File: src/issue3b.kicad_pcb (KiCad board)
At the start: 2 copper layers, 213.1 x 129 mm, 201 parts, among them IC1 ULA, IC10 4116, IC11 4116, IC12 4116, IC13 4116, IC14 LM1889, IC15 4532, IC16 4532, IC17 4532, IC18 4532, IC19 4532, IC2 Z80, IC20 4532, IC21 4532, IC22 4532, IC23 LS32, IC24 LS00, IC25 LS157, IC26 LS157, IC3 LS157, IC4 LS157, IC5 ROM, IC6 4116, IC7 4116, IC8 4116, IC9 4116, J7 Barrel_Jack_MountingPin, T1 Transformer_1P_1S, X1 14Mhz, X2 4.43Mhz

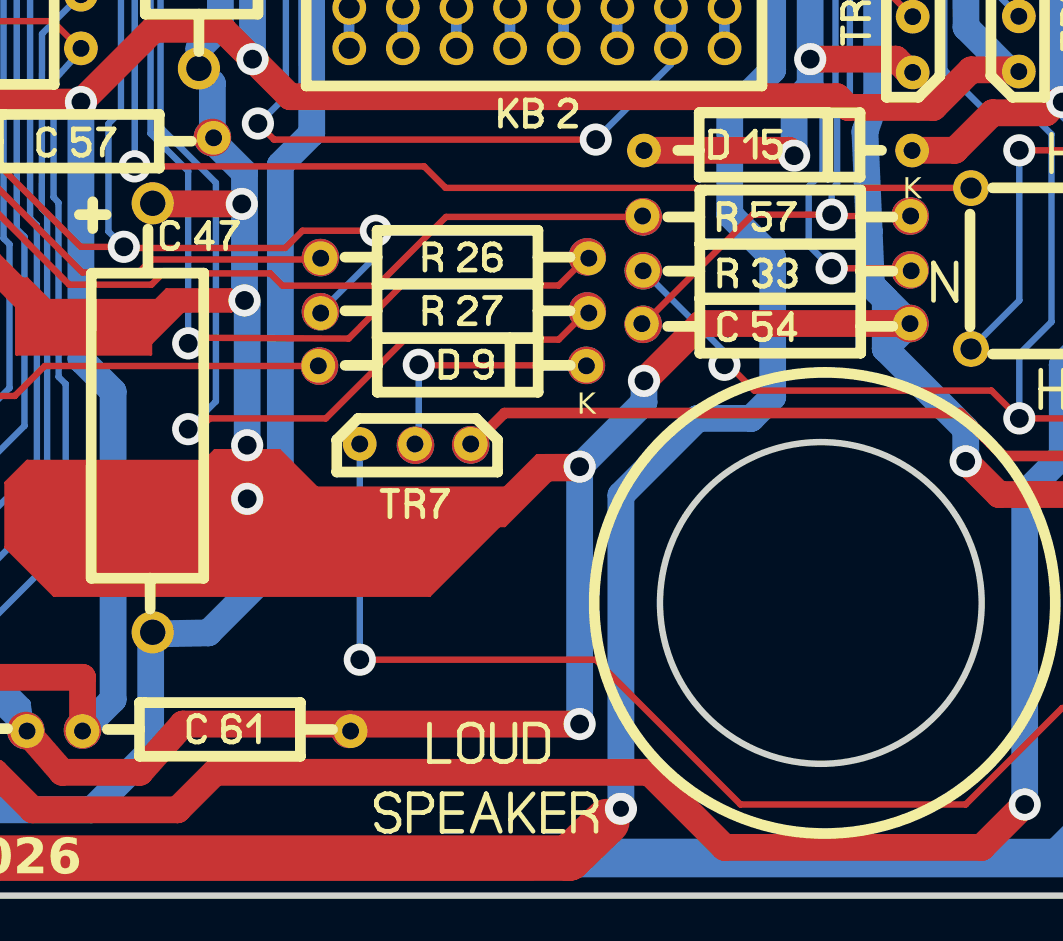
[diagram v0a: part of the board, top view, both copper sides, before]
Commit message: extra 3d parts from Dee inc heat sink.
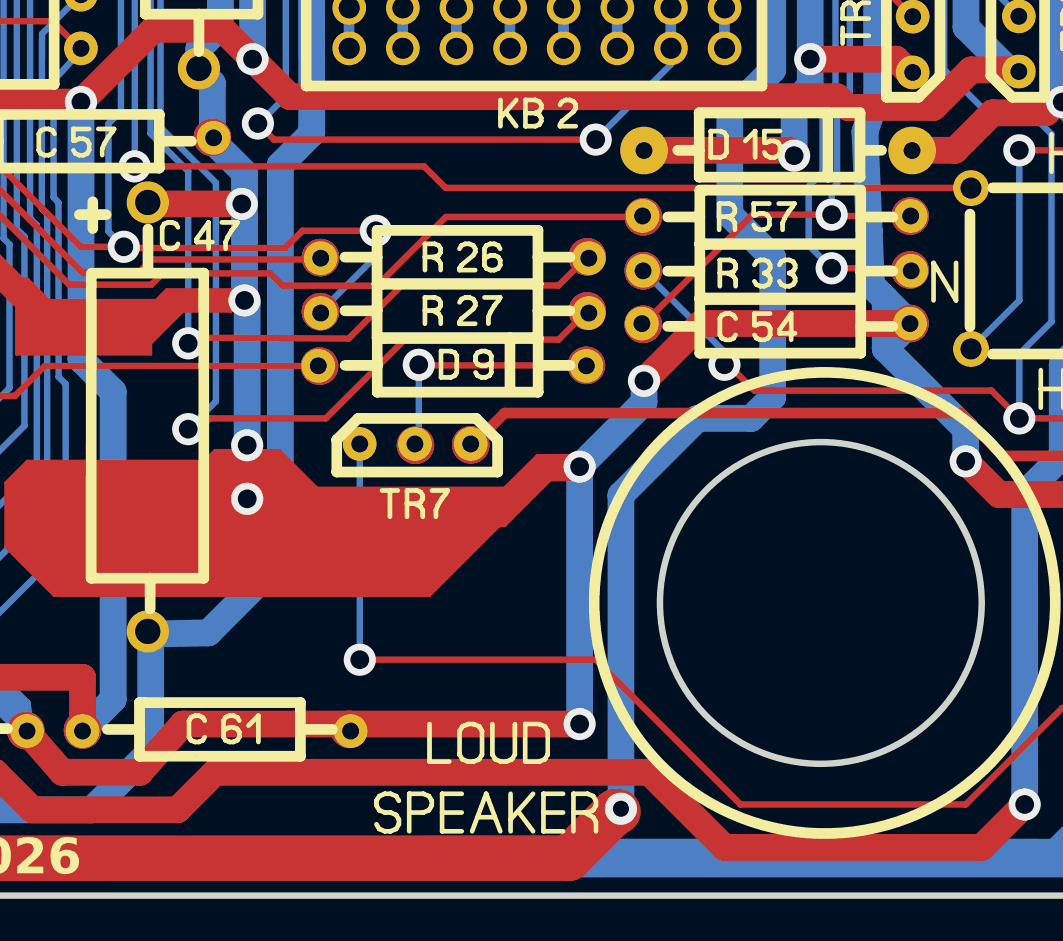
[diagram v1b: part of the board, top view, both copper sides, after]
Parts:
- moved C47 0.24 mm to (201.8, 122.8)
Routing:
- net +12VA: track 430.1 -> 430.8 mm
